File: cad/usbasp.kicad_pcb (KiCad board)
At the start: 2 copper layers, 72.4 x 40.6 mm, 33 parts, among them J1 USB_B, J2 UISP, J3 SLOW-SCK, J4 SELF-PRG, SW1 5V-3V3, SW2 V-TARGET, U1 AMS1117-3.3, U2 ATmega88-20PU, Y1 12MHz

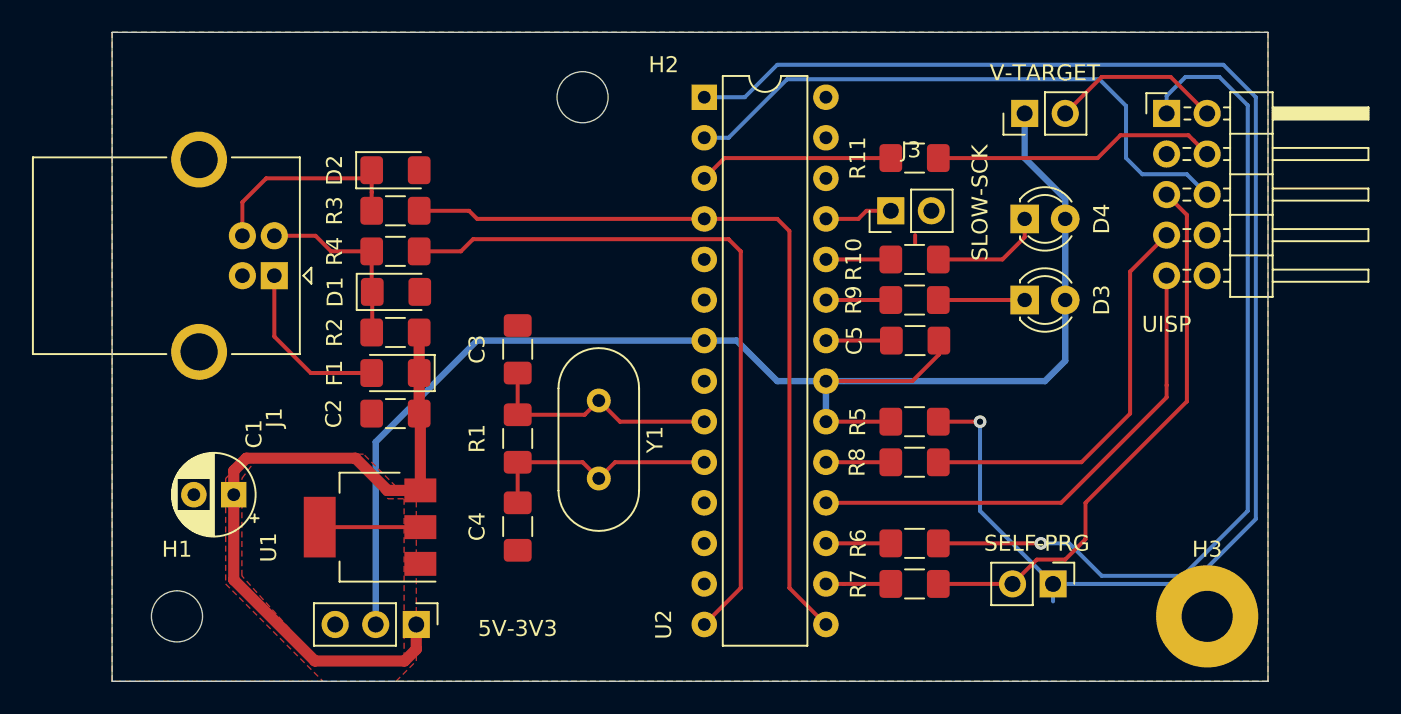
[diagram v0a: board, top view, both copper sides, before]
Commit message: Schematic: add 3.3v support
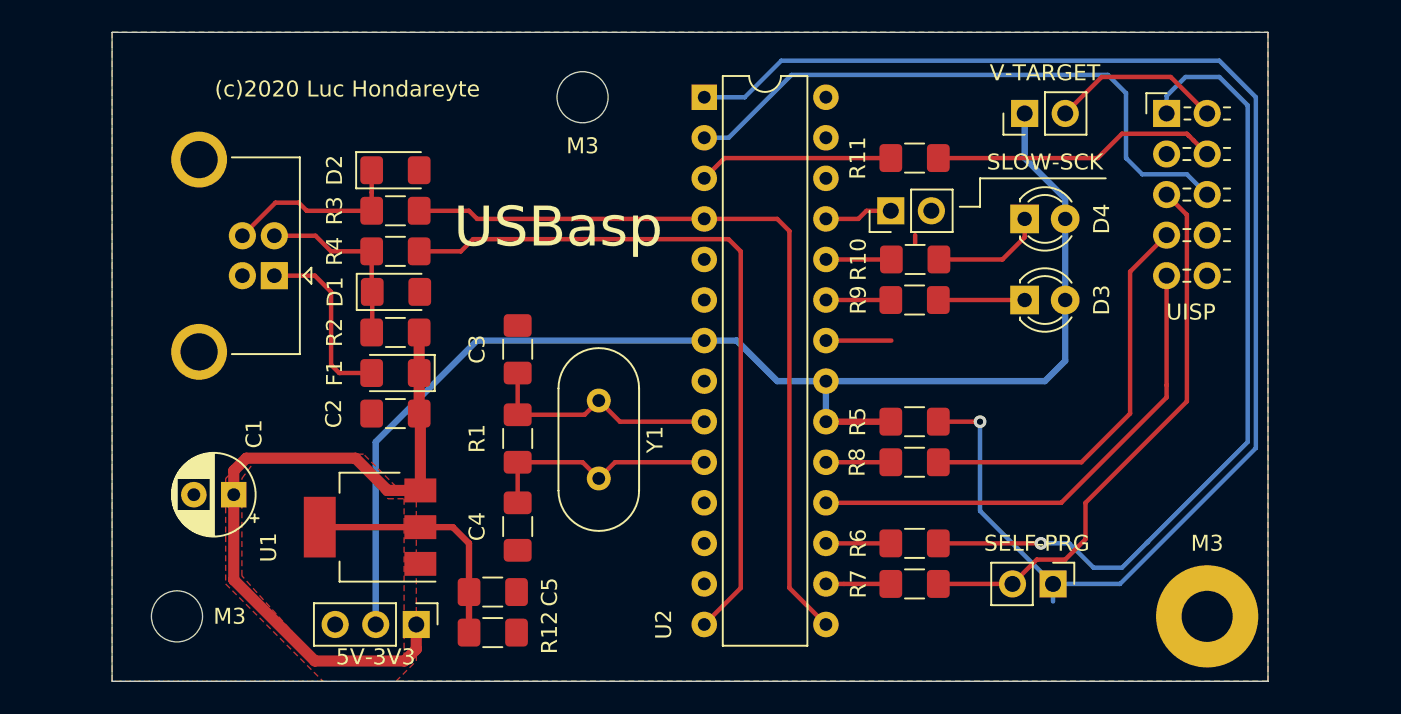
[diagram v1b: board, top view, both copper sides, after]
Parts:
- added R12: 220k, Resistor_SMD:R_1206_3216Metric_Pad1.42x1.75mm_HandSolder, F.Cu at (125.4, 70.6)
- R10, R9: value 1k -> 470R
- moved C5 30.8 mm to (125.4, 68.1), turned to 180 degrees
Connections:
- C5 pad 2: VCC -> +3V3
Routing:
- net +3V3: track 6.30 -> 15.4 mm
- net VCC: track 90.6 -> 82.0 mm
- net Net-(J2-Pad1): track 54.7 -> 51.9 mm
- net /~RESET: track 92.8 -> 90.4 mm
- net Net-(D2-Pad1): track 13.4 -> 11.7 mm
- net /PD0: track 37.9 -> 38.6 mm
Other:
- net class 3v3 added: clearance 0.2, trace_width 0.4, via_dia 0.8, via_drill 0.4
- net class Default: trace_width 0.25 -> 0.28
- board text added: "(c)2020 Luc Hondareyte"
- board text added: "USBasp"

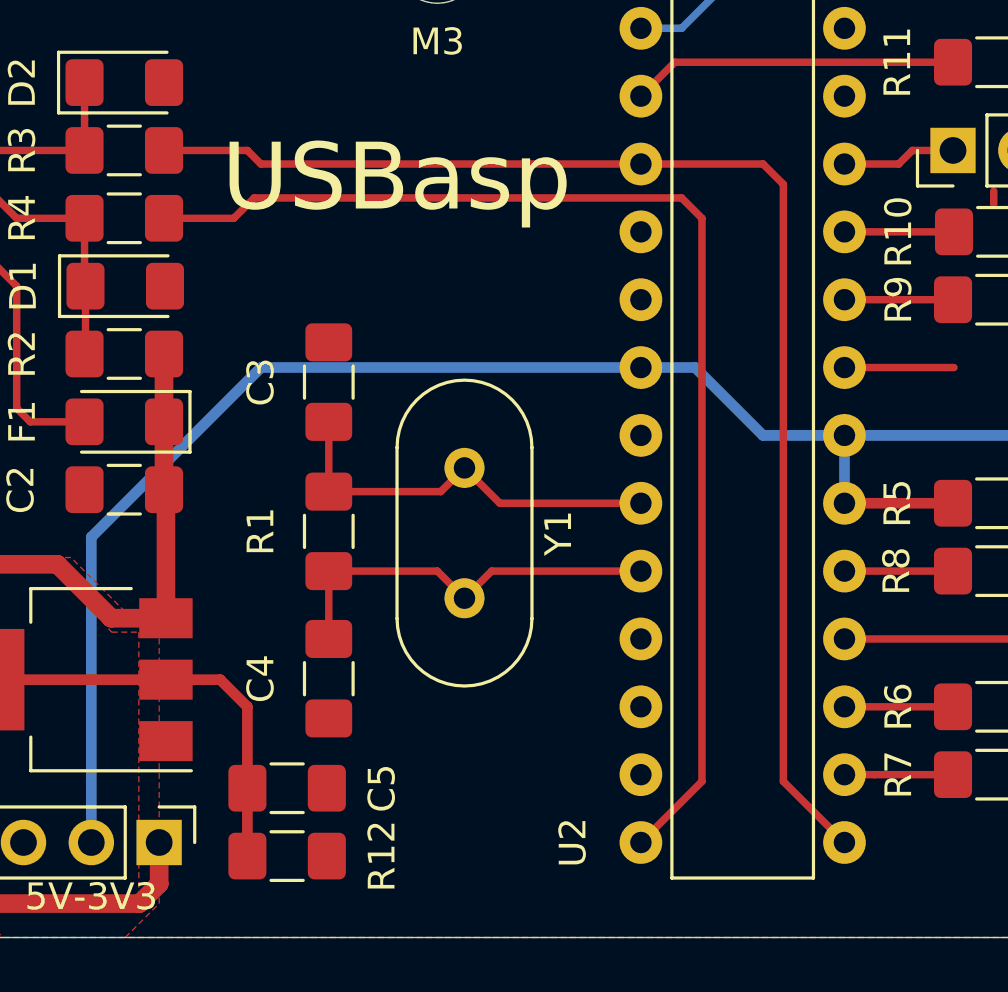
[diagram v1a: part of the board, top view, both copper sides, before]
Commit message: cad: update USB connector 3D model.
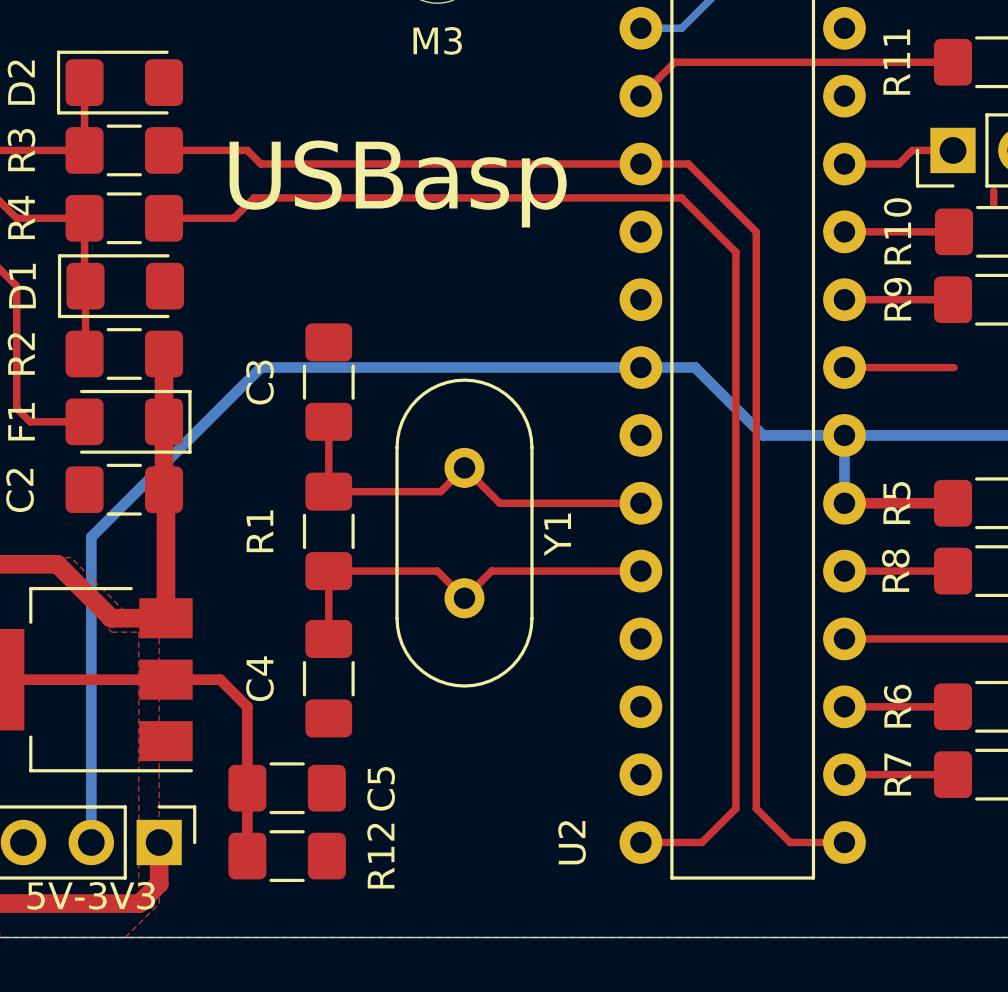
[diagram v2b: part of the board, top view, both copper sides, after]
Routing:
- net /DATA-: track 45.1 -> 47.5 mm
